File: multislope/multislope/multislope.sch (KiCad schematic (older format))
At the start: 36 parts, among them P1 CONN_1, P2 CONN_1, P3 CONN_1, P4 CONN_1, P5 CONN_8, P6 CONN_1, U1 A9_REFERENCE, U2 LT1013, U4 DG419, U5 ad711, U6 ad711, U7 ad711, U8 DG417

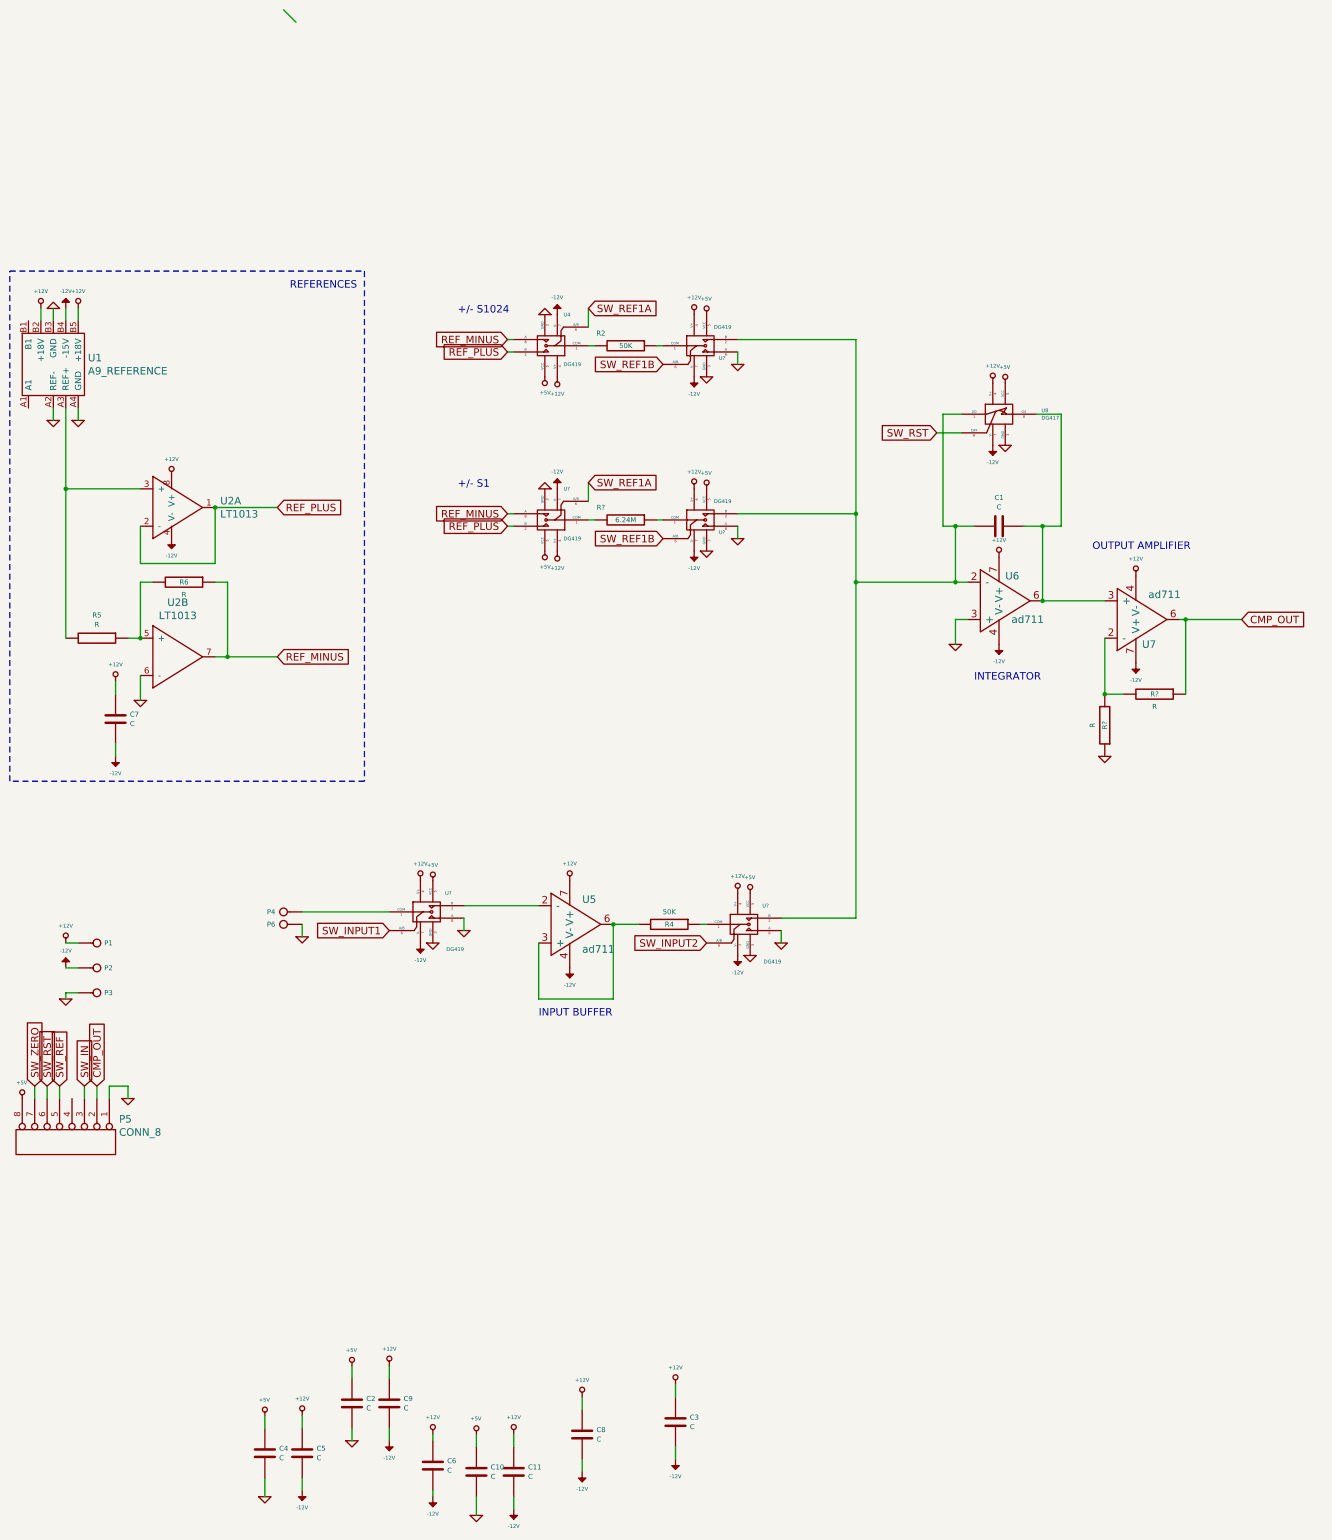
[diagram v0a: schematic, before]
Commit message: Trying FETs, two opamps in integrator
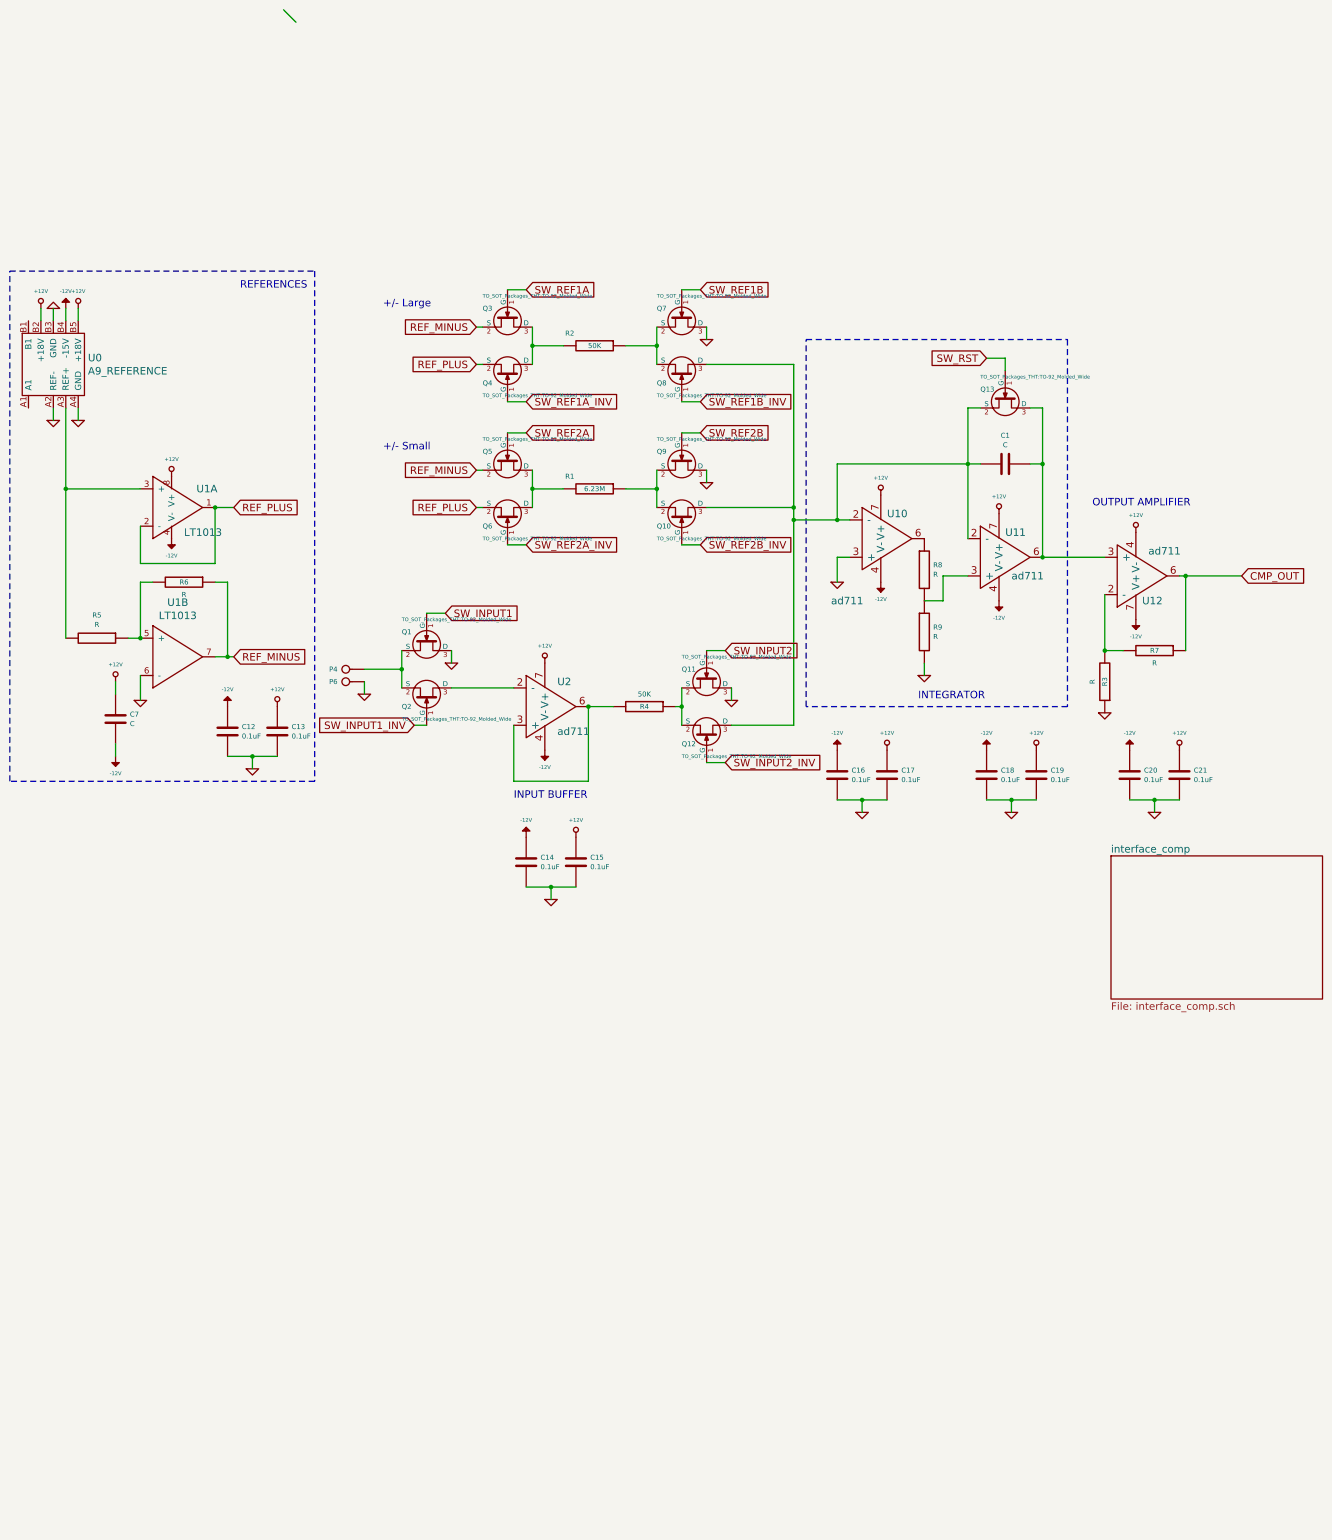
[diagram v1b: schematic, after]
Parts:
- removed C10, C11, C2, C3, C4, C5, C6, C8, C9: C, Capacitors_THT:C_Disc_D7.5mm_W4.4mm_P5.00mm, symbol device:C
- removed P1, P2, P3: CONN_1, 4mm_banana:4mm_banana, symbol conn:CONN_1
- removed P5: CONN_8, symbol conn:CONN_8
- removed R?: 6.24M, Resistors_THT:R_Axial_DIN0207_L6.3mm_D2.5mm_P10.16mm_Horizontal, symbol device:R
- removed U4, U? (x5): DG419, symbol analog_switches:DG419
- removed U8: DG417, symbol analog_switches:DG417
- added C12, C13, C14, C15, C16, C17, C18, C19, C20, C21: 0.1uF, Capacitors_SMD:C_1206_HandSoldering, symbol device:C
- added Q1, Q10, Q11, Q12, Q13, Q2, Q3, Q4, Q5, Q6, Q7, Q8, Q9: BF245A, TO_SOT_Packages_THT:TO-92_Molded_Wide, symbol transistors:BF245A
- added R1: 6.23M, Resistors_THT:R_Axial_DIN0207_L6.3mm_D2.5mm_P10.16mm_Horizontal, symbol device:R
- added R8, R9: R, Resistors_THT:R_Axial_DIN0207_L6.3mm_D2.5mm_P10.16mm_Horizontal, symbol device:R
- added U10: ad711, Housings_DIP:DIP-8_W7.62mm, symbol AD711:ad711
- C1, C7: footprint Capacitors_THT:C_Disc_D7.5mm_W4.4mm_P5.00mm -> Capacitors_SMD:C_1206_HandSoldering
- U1: renamed from U2; footprint (none) -> Housings_DIP:DIP-8_W7.62mm
- gave numbers to parts that had none: 2
- renumbered U1 to U0, U6 to U11, U7 to U12, U5 to U2
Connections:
- net +12V: now also C13.1, C15.1, C17.1, C19.1, C21.1, U10.7 (V+)
- net -12V: now also C12.1, C14.1, C16.1, C18.1, C20.1, U10.4 (V-)
- net GND: now also C12.2, C13.2, C14.2, C15.2, C16.2, C17.2, C18.2, C19.2, C20.2, C21.2, Q1.3 (D), Q11.3 (D), Q7.3 (D), Q9.3 (D), R9.2, U10.3 (+); no longer U11.3 (+)
- net REF_MINUS: now also Q3.2 (S), Q5.2 (S)
- net REF_PLUS: now also Q4.2 (S), Q6.2 (S)
- net SW_INPUT1: now also Q1.1 (G)
- net SW_INPUT2: now also Q11.1 (G)
- net SW_REF1A: now also Q3.1 (G)
- net SW_REF1B: now also Q7.1 (G)
- net SW_RST: now also Q13.1 (G)
- net at P4.1: now also Q1.2 (S), Q2.2 (S)
- net at R4.1: now also Q11.2 (S), Q12.2 (S)
- net at R2.1: now also Q7.2 (S), Q8.2 (S)
- net at R2.2: now also Q3.3 (D), Q4.3 (D)
- net at C1.1, U11.6, U12.3 (+): now also Q13.3 (D)
- net at C1.2, U11.2 (-): now also Q10.3 (D), Q12.3 (D), Q13.2 (S), Q8.3 (D), U10.2 (-)
- net at U2.2 (-): now also Q2.3 (D)
- new net: R8.2, R9.1, U11.3 (+)
- new net: Q10.2 (S), Q9.2 (S), R1.1
- new net: Q5.3 (D), Q6.3 (D), R1.2
- new net: R8.1, U10.6
- new net SW_INPUT1_INV: Q2.1 (G)
- new net SW_INPUT2_INV: Q12.1 (G)
- new net SW_REF1A_INV: Q4.1 (G)
- new net SW_REF1B_INV: Q8.1 (G)
- new net SW_REF2A: Q5.1 (G)
- new net SW_REF2A_INV: Q6.1 (G)
- new net SW_REF2B: Q9.1 (G)
- new net SW_REF2B_INV: Q10.1 (G)
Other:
- note added: "+/- Large"
- note added: "+/- Small"
- note removed: "+/- S1"
- note removed: "+/- S1024"
- moved on the sheet: C1, P4, P6, R2, R3, R4, R7, U11, U12, U2

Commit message: current multislope
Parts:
- removed Q1, Q10, Q11, Q12, Q13, Q2, Q3, Q4, Q5, Q6, Q7, Q8, Q9: BF245A, TO_SOT_Packages_THT:TO-92_Molded_Wide, symbol transistors:BF245A
- added C1000, C1001, C1010, C1011, C1020, C1021, C1030, C1031, C2000, C2001, C2020, C2021, C31, C32: 10nF, Capacitors_SMD:C_1206_HandSoldering, symbol device:C
- added R101: 50K, Resistors_THT:R_Axial_DIN0207_L6.3mm_D2.5mm_P10.16mm_Horizontal, symbol device:R
- added R102: 6.23M, Resistors_THT:R_Axial_DIN0207_L6.3mm_D2.5mm_P10.16mm_Horizontal, symbol device:R
- added U100, U101, U102, U103, U200, U202: DG419, Housings_SSOP:MSOP-8_3x3mm_Pitch0.65mm, symbol analog_switches:DG419
- added U16: DG417, Housings_SSOP:MSOP-8_3x3mm_Pitch0.65mm, symbol analog_switches:DG417
- renumbered C14 to C2010, C15 to C2011, R2 to R100, R1 to R103, R4 to R200, U2 to U201
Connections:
- net +12V: now also C1000.1, C1010.1, C1020.1, C1030.1, C2000.1, C2020.1, C31.1, U100.4 (V+), U101.4 (V+), U102.4 (V+), U103.4 (V+), U16.4 (V+), U200.4 (V+), U202.4 (V+)
- net -12V: now also U100.7 (V-), U101.7 (V-), U102.7 (V-), U103.7 (V-), U16.7 (V-), U200.7 (V-), U202.7 (V-)
- net GND: now also C1000.2, C1001.2, C1010.2, C1011.2, C1020.2, C1021.2, C1030.2, C1031.2, C2000.2, C2001.2, C2020.2, C2021.2, C31.2, C32.2, U100.3 (GND), U100.8 (A), U101.3 (GND), U101.8 (A), U102.3 (GND), U102.8 (A), U103.3 (GND), U103.8 (A), U16.3 (GND), U200.2 (B), U200.3 (GND), U202.3 (GND), U202.8 (A)
- net REF_MINUS: now also R100.2, R102.2
- net REF_PLUS: now also R103.2, R101.2
- net SW_INPUT1: now also U200.6 (A/B)
- net SW_INPUT2: now also U202.6 (A/B)
- net SW_REF1A: now also U100.6 (A/B)
- net SW_REF1B: now also U101.6 (A/B)
- net SW_REF2A: now also U102.6 (A/B)
- net SW_REF2B: now also U103.6 (A/B)
- net SW_RST: now also U16.6 (OFF)
- net at P4.1: now also U200.8 (A)
- net at R200.1: now also U202.1 (COM)
- net at R100.1: now also U100.1 (COM)
- net at C1.1, U11.6, U12.3 (+): now also U16.8 (O/I)
- net at C1.2, U10.2 (-), U11.2 (-): now also U100.2 (B), U101.2 (B), U102.2 (B), U103.2 (B), U16.1 (I/O), U202.2 (B)
- net at U201.2 (-): now also U200.1 (COM)
- net at R103.1: now also U103.1 (COM)
- new net: R101.1, U101.1 (COM)
- new net: R102.1, U102.1 (COM)
- new net +5V: C1001.1, C1011.1, C1021.1, C1031.1, C2001.1, C2021.1, C32.1, U100.5 (VCC), U101.5 (VCC), U102.5 (VCC), U103.5 (VCC), U16.5 (VCC), U200.5 (VCC), U202.5 (VCC)
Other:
- moved on the sheet: P4, P6, R100, R103

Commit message: DDC112 board, multislope and various other updates it seems
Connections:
- net +12V: now also U12.7 (V+); no longer U12.4 (V-)
- net -12V: now also U12.4 (V-); no longer U12.7 (V+)
- net GND: now also U1.5 (+); no longer U1.6 (-)
- net at R200.2, U201.6: now also U201.2 (-); no longer U201.3 (+)
- net at R5.1, R6.2: now also U1.6 (-); no longer U1.5 (+)
- net at U200.1 (COM): now also U201.3 (+); no longer U201.2 (-)
- no-connect marks 0 -> 1
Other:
- note added: "Wrong way round on layout?"
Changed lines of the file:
@@
 L power:+12V #PWR030
 U 1 1 5A380F33
-P 4800 3650
-F 0 "#PWR030" H 4800 3600 20  0001 C CNN
-F 1 "+12V" H 4800 3788 30  0000 C CNN
-F 2 "" H 4800 3650 60  0001 C CNN
-F 3 "" H 4800 3650 60  0001 C CNN
-	1    4800 3650
-	1    0    0    -1
-$EndComp
-$Comp
-L power:-12V #PWR031
-U 1 1 5A380F39
 P 4800 4350
-F 0 "#PWR031" H 4800 4480 20  0001 C CNN
-F 1 "-12V" H 4800 4487 30  0000 C CNN
+F 0 "#PWR030" H 4800 4300 20  0001 C CNN
+F 1 "+12V" H 4800 4488 30  0000 C CNN
 F 2 "" H 4800 4350 60  0001 C CNN
 F 3 "" H 4800 4350 60  0001 C CNN
 	1    4800 4350
 	-1   0    0    1
+$EndComp
+$Comp
+L power:-12V #PWR031
+U 1 1 5A380F39
+P 4800 3650
+F 0 "#PWR031" H 4800 3780 20  0001 C CNN
+F 1 "-12V" H 4800 3787 30  0000 C CNN
+F 2 "" H 4800 3650 60  0001 C CNN
+F 3 "" H 4800 3650 60  0001 C CNN
+	1    4800 3650
+	1    0    0    -1
 $EndComp
 $Comp
@@
 F 3 "" H 4750 4000 60  0001 C CNN
 	1    4750 4000
-	1    0    0    -1
+	1    0    0    1
 $EndComp
 $Comp
 L power:-12V #PWR042
 U 1 1 5A430DAA
+P 9550 2600
+F 0 "#PWR042" H 9550 2730 20  0001 C CNN
+F 1 "-12V" H 9550 2737 30  0000 C CNN
+F 2 "" H 9550 2600 60  0001 C CNN
+F 3 "" H 9550 2600 60  0001 C CNN
+	1    9550 2600
+	1    0    0    -1
+$EndComp
+$Comp
+L power:+12V #PWR043
+U 1 1 5A430E29
 P 9550 3300
-F 0 "#PWR042" H 9550 3430 20  0001 C CNN
-F 1 "-12V" H 9550 3437 30  0000 C CNN
+F 0 "#PWR043" H 9550 3250 20  0001 C CNN
+F 1 "+12V" H 9550 3438 30  0000 C CNN
 F 2 "" H 9550 3300 60  0001 C CNN
 F 3 "" H 9550 3300 60  0001 C CNN
 	1    9550 3300
 	-1   0    0    1
-$EndComp
-$Comp
-L power:+12V #PWR043
-U 1 1 5A430E29
-P 9550 2600
-F 0 "#PWR043" H 9550 2550 20  0001 C CNN
-F 1 "+12V" H 9550 2738 30  0000 C CNN
-F 2 "" H 9550 2600 60  0001 C CNN
-F 3 "" H 9550 2600 60  0001 C CNN
-	1    9550 2600
-	1    0    0    -1
 $EndComp
 $Comp
@@
 F 3 "" H 1800 3600 60  0001 C CNN
 	2    1800 3600
-	1    0    0    -1
+	1    0    0    1
 $EndComp
 Wire Wire Line
@@
 	0    -1   -1   0
 $EndComp
+NoConn ~ 11000 3850
+Text Notes 7250 1000 0    60   ~ 0
+Wrong way round on layout?
 $EndSCHEMATC
